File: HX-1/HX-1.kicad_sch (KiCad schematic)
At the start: 33 parts, among them J1 Conn_01x02_Socket, P1 USB_C_Plug_USB2.0, SW1 SW_SPDT, U1 STM32H723ZGT6

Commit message: add crystal circuitry and dedicated sheets for comms and power
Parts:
- added C22, C23: 10pF, Capacitor_SMD:C_0603_1608Metric, symbol Device:C
- added Y1: 16MHz, Crystal:Crystal_SMD_3225-4Pin_3.2x2.5mm, symbol Device:Crystal_GND24
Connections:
- net GND: now also C22.2, C23.1, Y1.2, Y1.4; no longer P1.A1 (GND), P1.A12 (GND), P1.B1 (GND), P1.B12 (GND), R3.2
- net RCC_OSC_IN: now also C23.2, Y1.1
- net RCC_OSC_OUT: now also C22.1, Y1.3
- new net: P1.A1 (GND), P1.A12 (GND), P1.B1 (GND), P1.B12 (GND)
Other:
- added sheet Communication and Debug (communication_debug.kicad_sch)
- added sheet Power Clock IO (power_clock_io.kicad_sch)
- note added: "(Load_C (10pF) - Stray_C (~5pF) ) * 2 = 10 pF"
- moved on the sheet: D1, D2, JP1, P1, R2, R3

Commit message: move components to correct sheets, change net labels to global
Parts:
- removed C22, C23: 10pF, Capacitor_SMD:C_0603_1608Metric, symbol Device:C
- removed D1, D2: D_Schottky, symbol Device:D_Schottky
- removed J1: Conn_01x02_Socket, symbol Connector:Conn_01x02_Socket
- removed JP1: 5V_USB_Solder_Bridge, Jumper:SolderJumper-2_P1.3mm_Bridged_RoundedPad1.0x1.5mm, symbol Jumper:SolderJumper_2_Bridged
- removed P1: USB_C_Plug_USB2.0, symbol Connector:USB_C_Plug_USB2.0
- removed R2: 10k, Resistor_SMD:R_0603_1608Metric, symbol Device:R
- removed R3: 20k, Resistor_SMD:R_0603_1608Metric, symbol Device:R
- removed Y1: 16MHz, Crystal:Crystal_SMD_3225-4Pin_3.2x2.5mm, symbol Device:Crystal_GND24
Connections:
- net +3.3V: now also U1.33 (VDDA)
- net +3.3VA: no longer U1.33 (VDDA)
- net GND: no longer U1.107 (VSS), U1.120 (VSS), U1.130 (VSS), U1.16 (VSS), U1.31 (VSSA), U1.38 (VSS), U1.51 (VSS), U1.61 (VSS), U1.83 (VSS), U1.94 (VSS)
- new net: U1.107 (VSS), U1.120 (VSS), U1.130 (VSS), U1.16 (VSS), U1.38 (VSS), U1.51 (VSS), U1.61 (VSS), U1.83 (VSS), U1.94 (VSS)
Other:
- note removed: "(Load_C (10pF) - Stray_C (~5pF) ) * 2 = 10 pF"
- note removed: "TODO: add VBUS LED"
- moved on the sheet: C1, C2, C21, R1, R4, SW1, U1

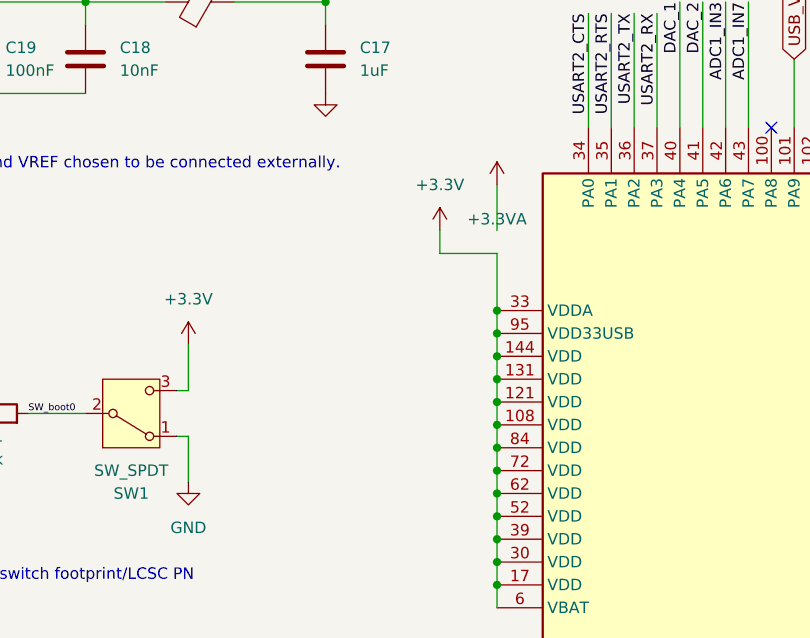
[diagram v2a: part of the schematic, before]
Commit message: add first draft of USB C design
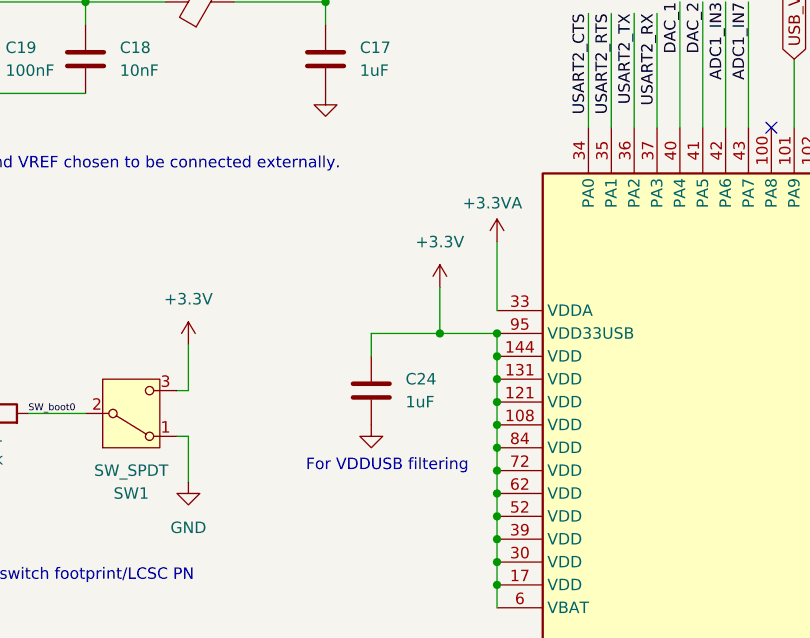
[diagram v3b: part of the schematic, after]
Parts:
- added C24: 1uF, Capacitor_SMD:C_0603_1608Metric, symbol Device:C
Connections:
- net +3.3V: now also C24.1; no longer U1.33 (VDDA)
- net +3.3VA: now also U1.33 (VDDA)
- net GND: now also C24.2
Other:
- note added: "For VDDUSB filtering"

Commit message: change almost all components to be basic jlcpcb parts
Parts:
- C1, C2: LCSC PN C126582 -> C23630
- C10, C11, C12, C13, C14, C15, C19, C21, C3, C4, C5, C6, C7, C8, C9: LCSC PN C478888 -> C14663
- C16: LCSC PN C70225 -> C19702
- C17, C20, C24: LCSC PN C93187 -> C15849
- FB1: value 120R -> 100R; footprint Resistor_SMD:R_0603_1608Metric -> Resistor_SMD:R_0805_2012Metric; LCSC PN C280478 -> C1015
- R1, R4: LCSC PN C3017715 -> C25804
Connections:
- net GND: now also U1.107 (VSS), U1.120 (VSS), U1.130 (VSS), U1.16 (VSS), U1.31 (VSSA), U1.38 (VSS), U1.51 (VSS), U1.61 (VSS), U1.83 (VSS), U1.94 (VSS)

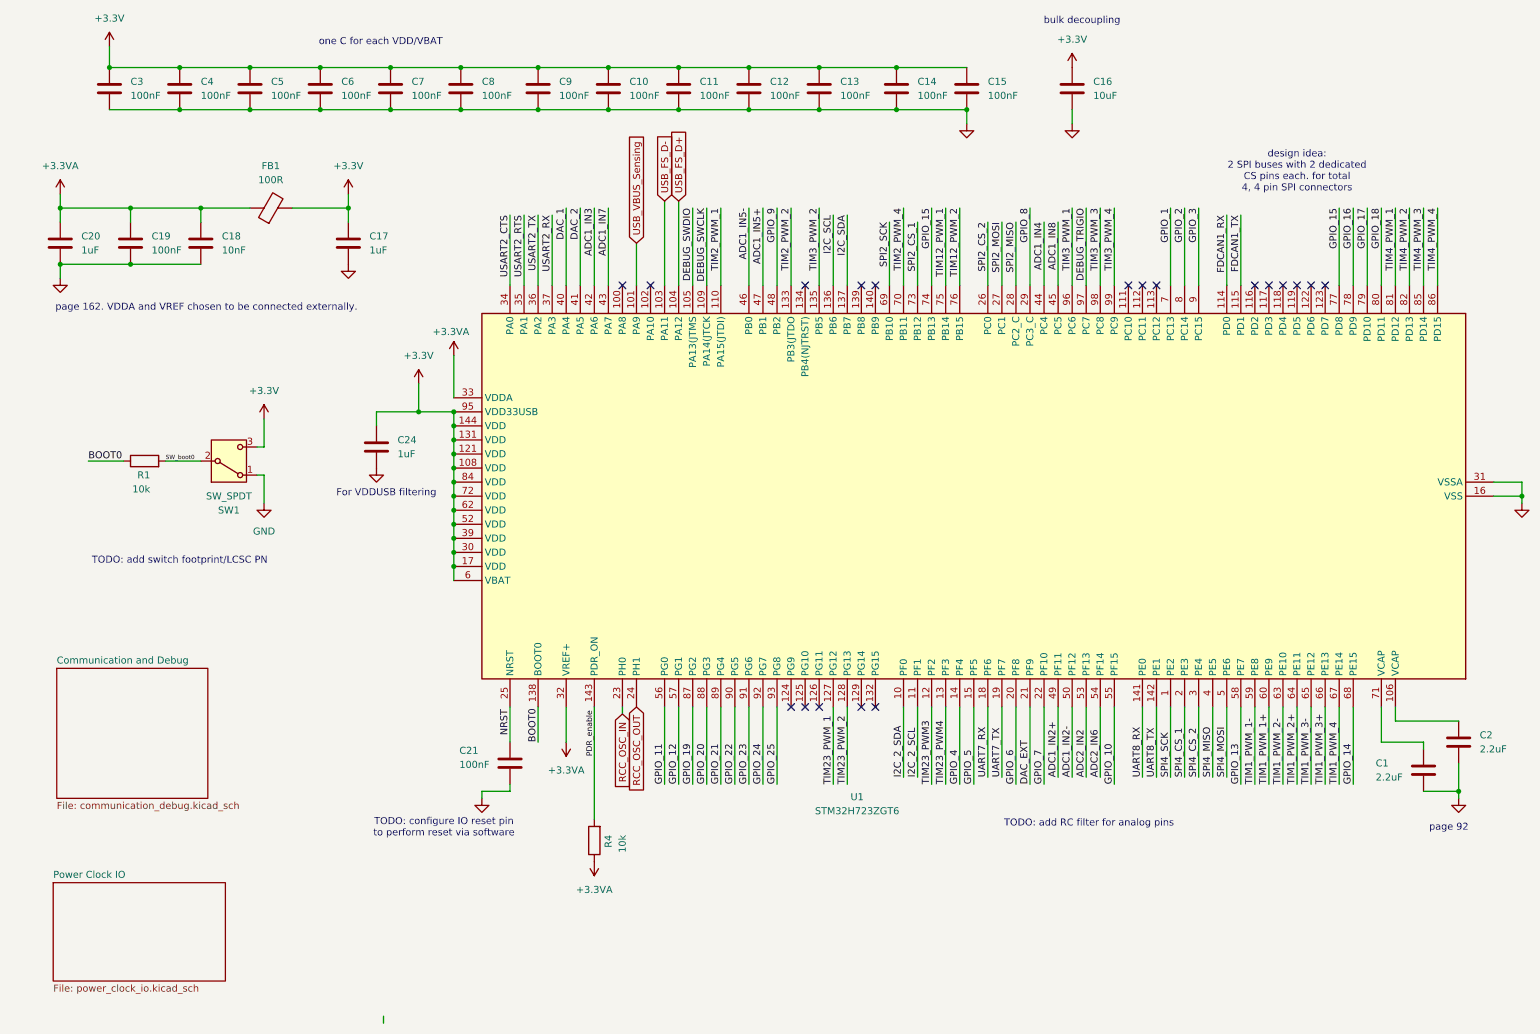
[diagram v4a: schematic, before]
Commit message: add mcu schematic file, change main to just link to other schematics. Update readme to show MCU schematic
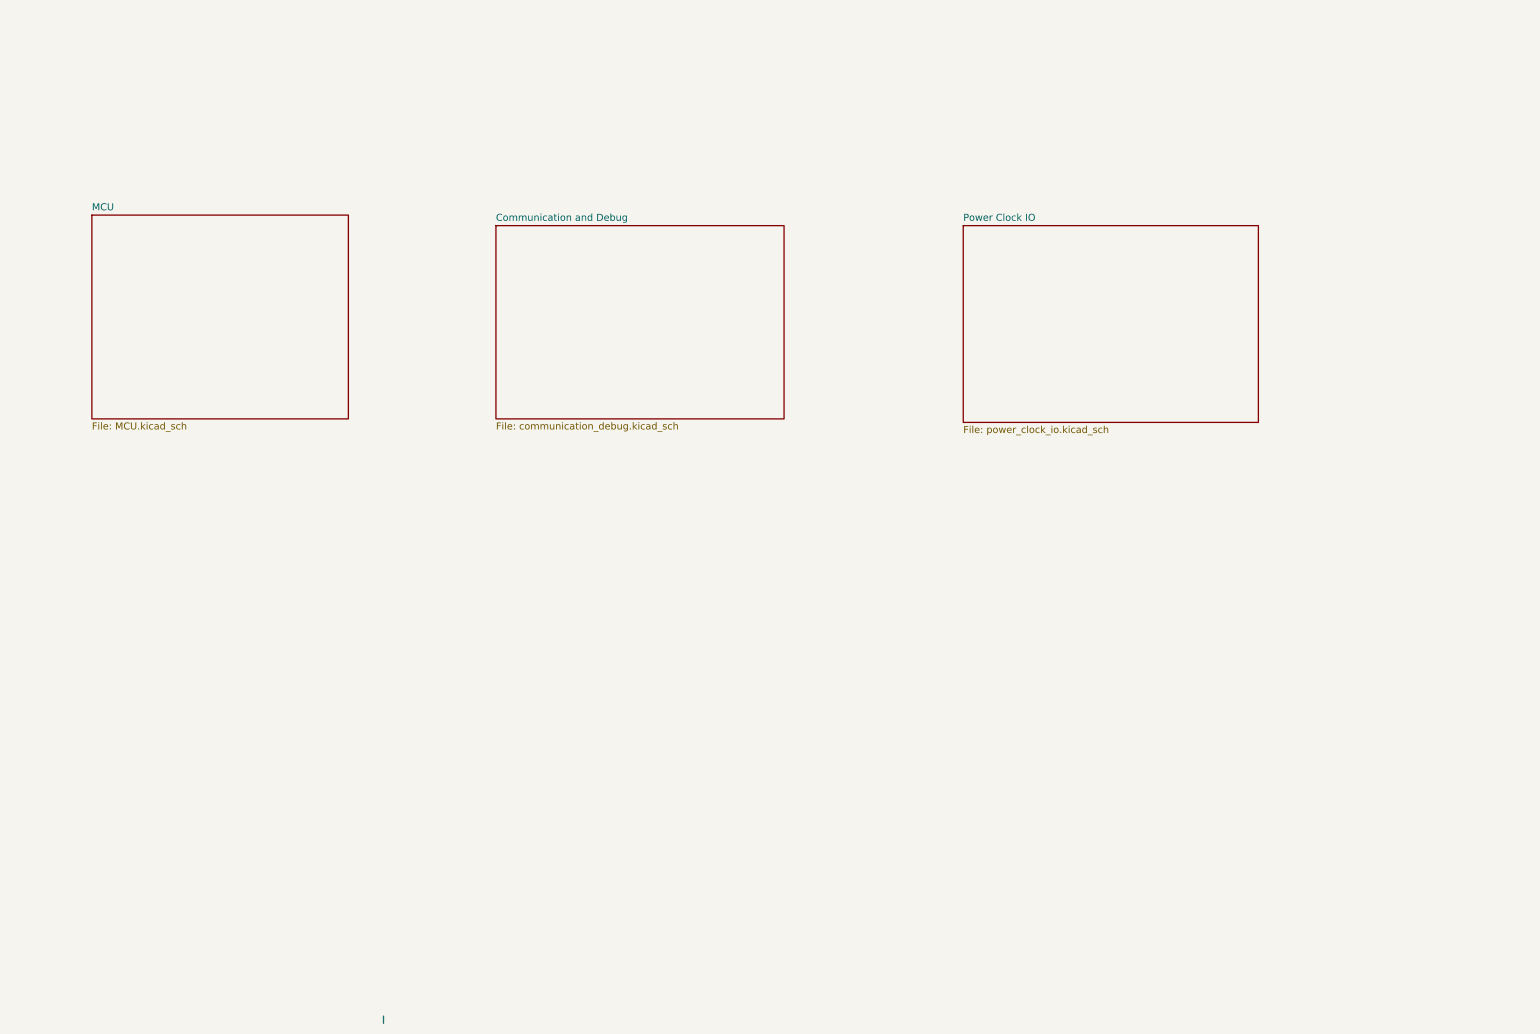
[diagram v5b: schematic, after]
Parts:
- removed C1, C2: 2.2uF, Capacitor_SMD:C_0603_1608Metric, symbol Device:C
- removed C10, C11, C12, C13, C14, C15, C19, C21, C3, C4, C5, C6, C7, C8, C9: 100nF, Capacitor_SMD:C_0603_1608Metric, symbol Device:C
- removed C16: 10uF, Capacitor_SMD:C_0603_1608Metric, symbol Device:C
- removed C17, C20, C24: 1uF, Capacitor_SMD:C_0603_1608Metric, symbol Device:C
- removed C18: 10nF, Capacitor_SMD:C_0603_1608Metric, symbol Device:C
- removed FB1: 100R, Resistor_SMD:R_0805_2012Metric, symbol Device:FerriteBead
- removed R1, R4: 10k, Resistor_SMD:R_0603_1608Metric, symbol Device:R
- removed SW1: SW_SPDT, symbol Switch:SW_SPDT
- removed U1: STM32H723ZGT6, Package_QFP:LQFP-144_20x20mm_P0.5mm, symbol MCU_ST_STM32H7:STM32H723ZGTx
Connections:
- no-connect marks 19 -> 0
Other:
- added sheet MCU (MCU.kicad_sch)
- note removed: "For VDDUSB filtering"
- note removed: "TODO: add RC filter for analog pins"
- note removed: "TODO: add switch footprint/LCSC PN"
- note removed: "TODO: configure IO reset pin to perform reset via software"
- note removed: "bulk decoupling"
- note removed: "design idea: 2 SPI buses with 2 dedicated CS pins each. for total 4, 4 pin SPI connectors"
- note removed: "one C for each VDD/VBAT"
- note removed: "page 162. VDDA and VREF chosen to be connected externally."
- note removed: "page 92"
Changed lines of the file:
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@@
 	(generator_version "8.0")
 	(paper "A4")
+	(wire
+		(pts
+			(xy 77.47 195.58) (xy 77.47 196.85)
+		)
+		(stroke
+			(width 0)
+			(type default)
+		)
+	)
+	(sheet
+		(at 182.245 52.705)
+		(size 53.34 35.56)
+		(fields_autoplaced yes)
+		(stroke
+			(width 0.1524)
+			(type solid)
+		)
+		(fill
+			(color 0 0 0 0.0000)
+		)
+		(property "Sheetname" "Power Clock IO"
+			(at 182.245 51.9934 0)
+			(effects
+				(font
+					(size 1.27 1.27)
+				)
+				(justify left bottom)
+			)
+		)
+		(property "Sheetfile" "power_clock_io.kicad_sch"
+			(at 182.245 88.8496 0)
+			(effects
+				(font
+					(size 1.27 1.27)
+				)
+				(justify left top)
+			)
+		)
+		(instances
+			(project "HX-1"
+				(path "/a3219989-2bf1-44ea-9412-fab86edfb39b"
+					(page "2")
+				)
+			)
+		)
+	)
+	(sheet
+		(at 24.765 50.8)
+		(size 46.355 36.83)
+		(fields_autoplaced yes)
+		(stroke
+			(width 0.1524)
+			(type solid)
+		)
+		(fill
+			(color 0 0 0 0.0000)
+		)
+		(property "Sheetname" "MCU"
+			(at 24.765 50.0884 0)
+			(effects
+				(font
+					(size 1.27 1.27)
+				)
+				(justify left bottom)
+			)
+		)
+		(property "Sheetfile" "MCU.kicad_sch"
+			(at 24.765 88.2146 0)
+			(effects
+				(font
+					(size 1.27 1.27)
+				)
+				(justify left top)
+			)
+		)
+		(instances
+			(project "HX-1"
+				(path "/a3219989-2bf1-44ea-9412-fab86edfb39b"
+					(page "4")
+				)
+			)
+		)
+	)
+	(sheet
+		(at 97.79 52.705)
+		(size 52.07 34.925)
+		(fields_autoplaced yes)
+		(stroke
+			(width 0.1524)
+			(type solid)
+		)
+		(fill
+			(color 0 0 0 0.0000)
+		)
+		(property "Sheetname" "Communication and Debug"
+			(at 97.79 51.9934 0)
+			(effects
+				(font
+					(size 1.27 1.27)
+				)
+				(justify left bottom)
+			)
+		)
+		(property "Sheetfile" "communication_debug.kicad_sch"
+			(at 97.79 88.2146 0)
+			(effects
+				(font
+					(size 1.27 1.27)
+				)
+				(justify left top)
+			)
+		)
+		(instances
+			(project "HX-1"
+				(path "/a3219989-2bf1-44ea-9412-fab86edfb39b"
+					(page "3")
+				)
+			)
+		)
+	)
+	(sheet_instances
+		(path "/"
+			(page "1")
+		)
+	)
+)

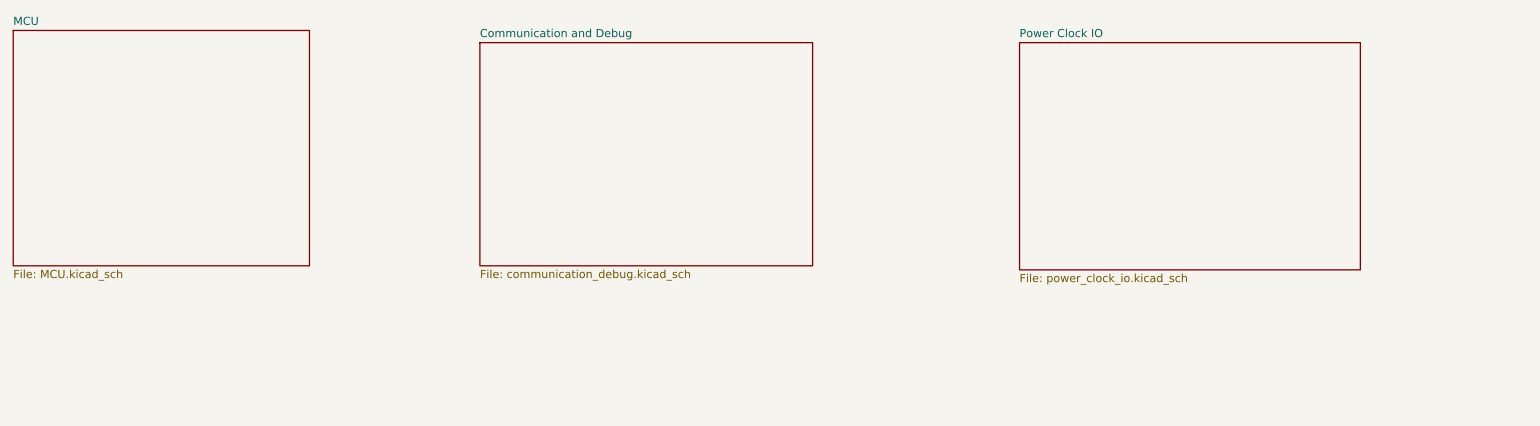
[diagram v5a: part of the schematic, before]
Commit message: change schematic file name and doc, script references
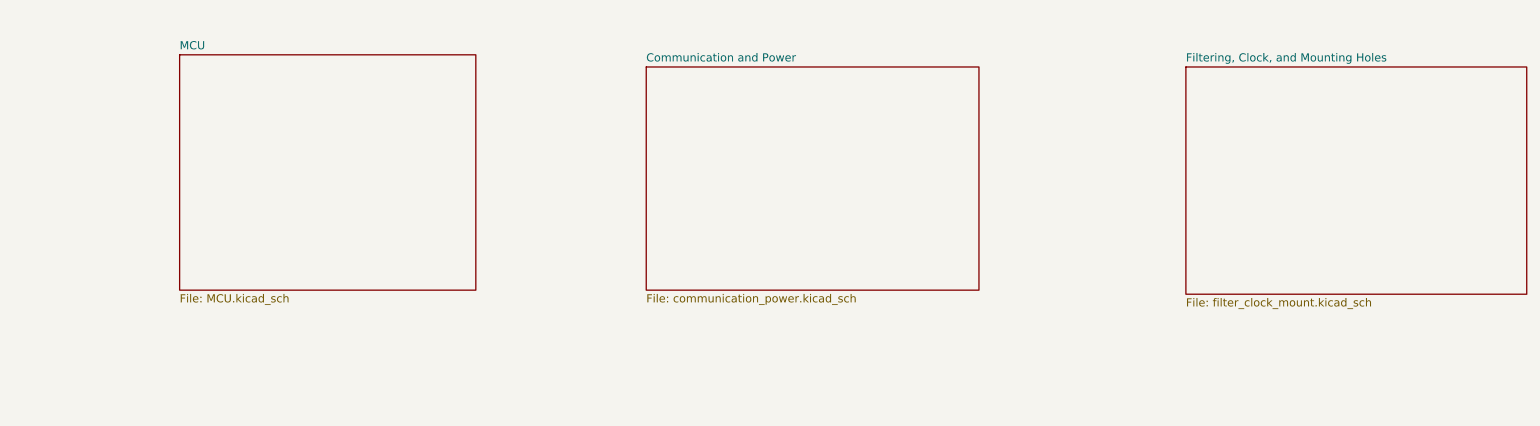
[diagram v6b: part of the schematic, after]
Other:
- sheet Communication and Debug renamed Communication and Power
- sheet Power Clock IO renamed Filtering, Clock, and Mounting Holes
- sheet Communication and Power: file communication_debug.kicad_sch -> communication_power.kicad_sch
- sheet Filtering, Clock, and Mounting Holes: file power_clock_io.kicad_sch -> filter_clock_mount.kicad_sch
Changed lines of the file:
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@@
 	)
 	(sheet
-		(at 182.245 52.705)
+		(at 208.28 56.515)
 		(size 53.34 35.56)
 		(fields_autoplaced yes)
@@
 			(color 0 0 0 0.0000)
 		)
-		(property "Sheetname" "Power Clock IO"
-			(at 182.245 51.9934 0)
+		(property "Sheetname" "Filtering, Clock, and Mounting Holes"
+			(at 208.28 55.8034 0)
 			(effects
 				(font
@@
 			)
 		)
-		(property "Sheetfile" "power_clock_io.kicad_sch"
-			(at 182.245 88.8496 0)
+		(property "Sheetfile" "filter_clock_mount.kicad_sch"
+			(at 208.28 92.6596 0)
 			(effects
 				(font
@@
 	)
 	(sheet
-		(at 24.765 50.8)
+		(at 50.8 54.61)
 		(size 46.355 36.83)
 		(fields_autoplaced yes)
@@
 		)
 		(property "Sheetname" "MCU"
-			(at 24.765 50.0884 0)
+			(at 50.8 53.8984 0)
 			(effects
 				(font
@@
 		)
 		(property "Sheetfile" "MCU.kicad_sch"
-			(at 24.765 88.2146 0)
+			(at 50.8 92.0246 0)
 			(effects
 				(font
@@
 	)
 	(sheet
-		(at 97.79 52.705)
+		(at 123.825 56.515)
 		(size 52.07 34.925)
 		(fields_autoplaced yes)
@@
 			(color 0 0 0 0.0000)
 		)
-		(property "Sheetname" "Communication and Debug"
-			(at 97.79 51.9934 0)
+		(property "Sheetname" "Communication and Power"
+			(at 123.825 55.8034 0)
 			(effects
 				(font
@@
 			)
 		)
-		(property "Sheetfile" "communication_debug.kicad_sch"
-			(at 97.79 88.2146 0)
+		(property "Sheetfile" "communication_power.kicad_sch"
+			(at 123.825 92.0246 0)
 			(effects
 				(font
